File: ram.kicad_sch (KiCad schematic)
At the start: 42 parts, among them IC11 HM514260AJ8, IC25 74ALS139, IC6 HM514260AJ8, U2 TXS0108EPW, U3 TXS0108EPW, U4 TXS0108EPW, U5 TXS0108EPW, U6 IS41LV16105D, U7 IS41LV16105D, U8 TXS0108EPW, U9 TXS0108EPW

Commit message: verify all component values vs TRM
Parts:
- C11, C12, C13, C17, C18, C19: value 100nF -> 100nF 20%
- C131: value 10uF -> 10uF 10V 20%
- C159, C165: value 47uF -> 47uF 10V
- C162: value 100nF -> 33nF
- IC25: value 74ALS139 -> 74HC139
- L15, L16: value 2R2 -> 1A 80R@100MHz
- R135: value 330R -> 330R 5% 0.1W
- R136: value 10K -> 10K 5% 0.1W
- RP2, RP4, RP5, RP6: value 68Rx8 -> 68Rx8 5%
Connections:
- net DRAM2_5V is gone; now on net DRAM_5V: C11.1, C12.1, C159.1, C18.1, IC11.1 (Vcc), IC11.21 (Vcc), IC11.6 (Vcc), L15.2
- net DRAM1_5V renamed DRAM_5V
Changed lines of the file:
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@@
 	)
 	(junction
+		(at 68.58 215.9)
+		(diameter 0)
+		(color 0 0 0 0)
+	)
+	(junction
 		(at 49.53 270.51)
 		(diameter 0)
@@
 	)
 	(junction
-		(at 81.28 215.9)
+		(at 62.23 215.9)
 		(diameter 0)
 		(color 0 0 0 0)
@@
 	(wire
 		(pts
+			(xy 62.23 215.9) (xy 68.58 215.9)
+		)
+		(stroke
+			(width 0)
+			(type default)
+		)
+	)
+	(wire
+		(pts
 			(xy 137.16 163.83) (xy 143.51 163.83)
 		)
@@
 		)
 	)
-	(wire
-		(pts
-			(xy 81.28 215.9) (xy 83.82 215.9)
-		)
-		(stroke
-			(width 0)
-			(type default)
-		)
-	)
 	(bus
 		(pts
@@
 		)
 	)
-	(label "DRAM2_5V"
+	(label "DRAM_5V"
 		(at 158.75 31.75 180)
 		(effects
@@
 		)
 	)
-	(label "DRAM1_5V"
+	(label "DRAM_5V"
 		(at 57.15 31.75 180)
 		(effects
@@
 		)
 	)
-	(label "DRAM1_5V"
-		(at 83.82 215.9 0)
-		(effects
-			(font
-				(size 1.27 1.27)
-			)
-			(justify left bottom)
-		)
-	)
 	(label "A9"
 		(at 398.78 140.97 0)
@@
 		)
 	)
-	(label "DRAM2_5V"
+	(label "DRAM_5V"
 		(at 35.56 262.89 0)
 		(effects
@@
 		)
 	)
-	(label "DRAM1_5V"
+	(label "DRAM_5V"
 		(at 22.86 262.89 180)
 		(effects
@@
 		)
 	)
-	(label "DRAM2_5V"
+	(label "DRAM_5V"
 		(at 46.99 215.9 180)
 		(effects
@@
 			)
 		)
-		(property "Value" "2R2"
+		(property "Value" "1A 80R@100MHz"
 			(at 34.29 260.3499 0)
 			(effects
@@
 			)
 		)
-		(property "Value" "47uF"
+		(property "Value" "47uF 10V"
 			(at 30.48 267.4238 0)
 			(effects
@@
 			)
 		)
-		(property "Value" "2R2"
+		(property "Value" "1A 80R@100MHz"
 			(at 24.13 260.3499 0)
 			(effects
@@
 			)
 		)
-		(property "Value" "330R"
+		(property "Value" "330R 5% 0.1W"
 			(at 200.66 275.59 90)
 			(effects
@@
 			)
 		)
-		(property "Value" "74ALS139"
+		(property "Value" "74HC139"
 			(at 223.52 260.35 0)
 			(effects
@@
 			)
 		)
-		(property "Value" "10uF"
+		(property "Value" "10uF 10V 20%"
 			(at 21.59 238.2138 0)
 			(effects
@@
 			)
 		)
-		(property "Value" "100nF"
+		(property "Value" "100nF 20%"
 			(at 76.454 214.63 90)
 			(effects
@@
 			)
 		)
-		(property "Value" "68Rx8"
+		(property "Value" "68Rx8 5%"
 			(at 148.59 203.2 90)
 			(effects
@@
 			)
 		)
-		(property "Value" "100nF"
+		(property "Value" "100nF 20%"
 			(at 82.804 214.63 90)
 			(effects
@@
 			)
 		)
-		(property "Value" "100nF"
+		(property "Value" "100nF 20%"
 			(at 69.85 214.884 90)
 			(effects
@@
 			)
 		)
-		(property "Value" "68Rx8"
+		(property "Value" "68Rx8 5%"
 			(at 148.59 147.32 90)
 			(effects
@@
 			)
 		)
-		(property "Value" "47uF"
+		(property "Value" "47uF 10V"
 			(at 20.32 267.4238 0)
 			(effects
@@
 			)
 		)
-		(property "Value" "74ALS139"
+		(property "Value" "74HC139"
 			(at 257.81 261.6199 0)
 			(effects
@@
 			)
 		)
-		(property "Value" "68Rx8"
+		(property "Value" "68Rx8 5%"
 			(at 148.59 231.14 90)
 			(effects
@@
 			)
 		)
-		(property "Value" "100nF"
+		(property "Value" "100nF 20%"
 			(at 50.8 214.884 90)
 			(effects
@@
 			)
 		)
-		(property "Value" "100nF"
+		(property "Value" "100nF 20%"
 			(at 57.15 214.884 90)
 			(effects
@@
 			)
 		)
-		(property "Value" "10K"
+		(property "Value" "10K 5% 0.1W"
 			(at 208.28 260.35 90)
 			(effects
@@
 			)
 		)
-		(property "Value" "100nF"
+		(property "Value" "33nF"
 			(at 246.3863 241.3 90)
 			(effects
@@
 			)
 		)
-		(property "Value" "74ALS139"
+		(property "Value" "74HC139"
 			(at 283.21 261.62 0)
 			(effects
@@
 			)
 		)
-		(property "Value" "100nF"
+		(property "Value" "100nF 20%"
 			(at 63.5 214.884 90)
 			(effects
@@
 			)
 		)
-		(property "Value" "68Rx8"
+		(property "Value" "68Rx8 5%"
 			(at 148.59 175.26 90)
 			(effects

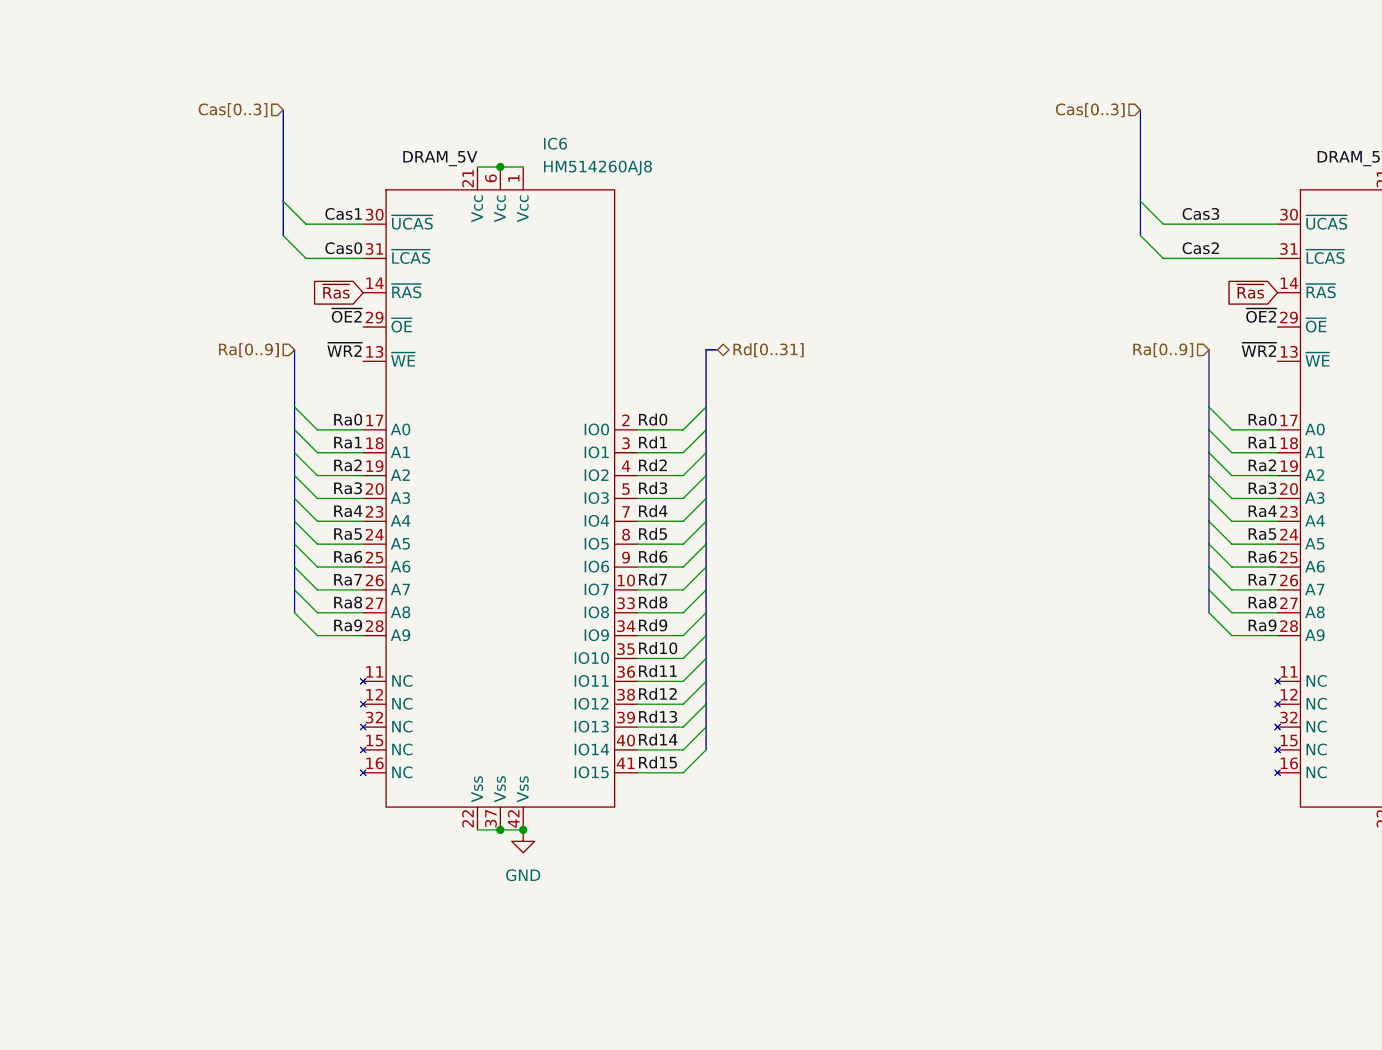
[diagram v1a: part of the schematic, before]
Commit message: fix qfp footprints, restore CAS filters
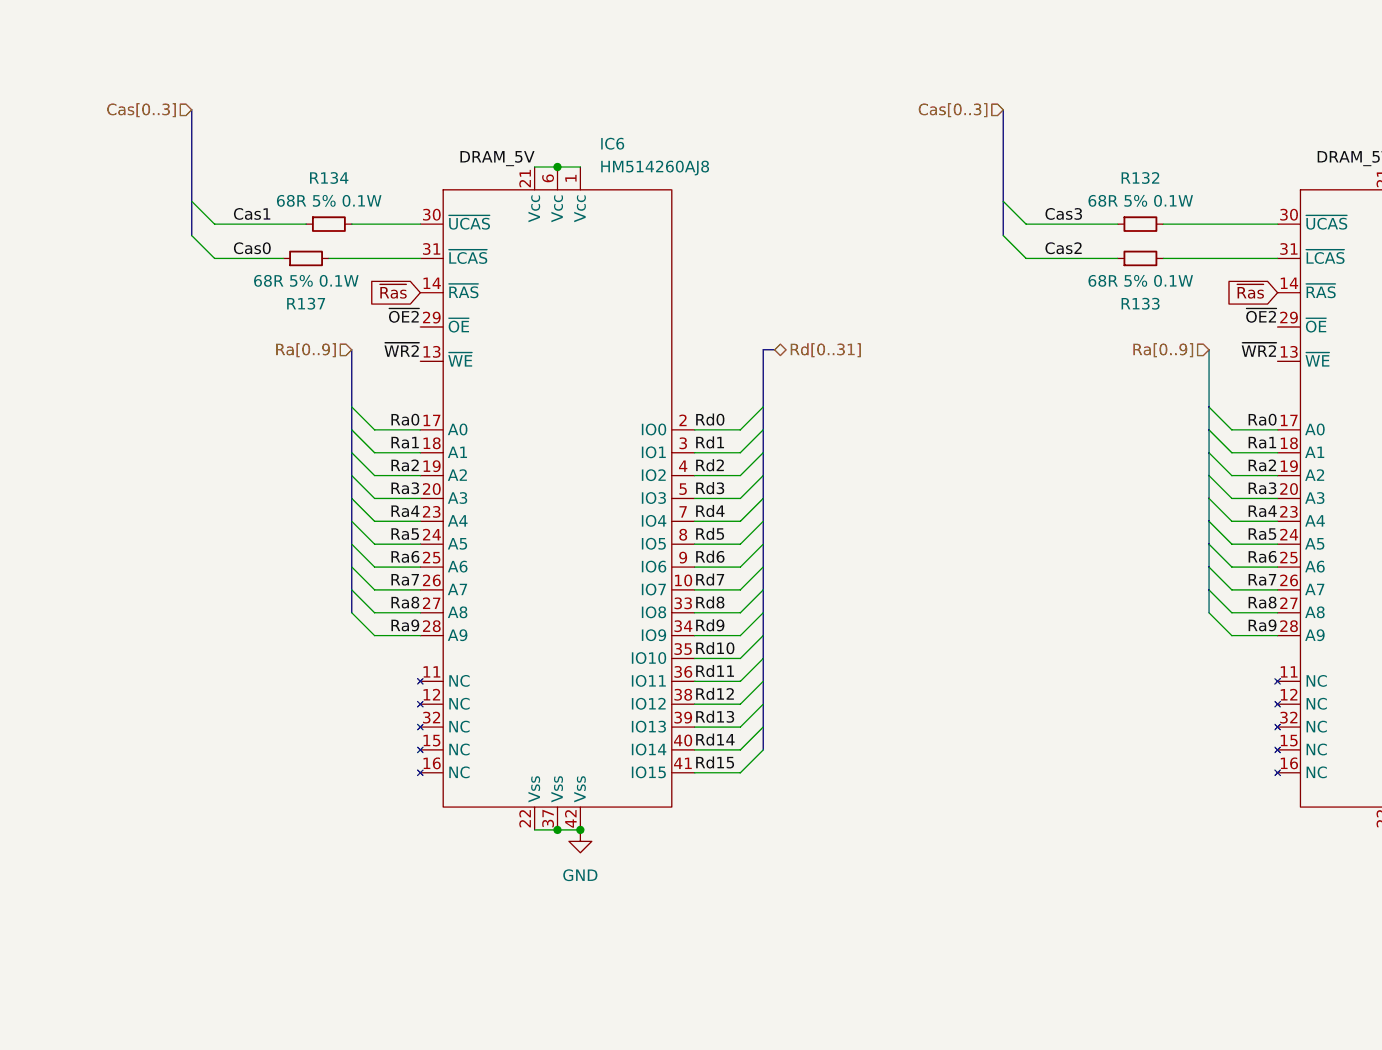
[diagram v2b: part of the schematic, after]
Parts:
- added R132, R133, R134, R137: 68R 5% 0.1W, Resistor_SMD:R_0805_2012Metric, symbol Device:R_Small
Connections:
- net Cas0: now also R137.1; no longer IC6.31 (~{LCAS})
- net Cas1: now also R134.1; no longer IC6.30 (~{UCAS})
- net Cas2: now also R133.1; no longer IC11.31 (~{LCAS})
- net Cas3: now also R132.1; no longer IC11.30 (~{UCAS})
- new net: IC6.31 (~{LCAS}), R137.2
- new net: IC11.30 (~{UCAS}), R132.2
- new net: IC11.31 (~{LCAS}), R133.2
- new net: IC6.30 (~{UCAS}), R134.2
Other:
- moved on the sheet: IC6

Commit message: revise cap footprint selection
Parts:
- C228: footprint Capacitor_THT:CP_Radial_D10.0mm_P7.50mm -> Capacitor_THT:CP_Radial_D8.0mm_P5.00mm
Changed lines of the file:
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@@
 			)
 		)
-		(property "Footprint" "Capacitor_THT:CP_Radial_D10.0mm_P7.50mm"
+		(property "Footprint" "Capacitor_THT:CP_Radial_D8.0mm_P5.00mm"
 			(at 29.21 237.49 0)
 			(effects
